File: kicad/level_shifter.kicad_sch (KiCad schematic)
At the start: 30 parts, among them U3 74LVC2T45GT, U4 74LVC2T45GT, U5 74LVC2T45GT, U6 74LVC2T45GT

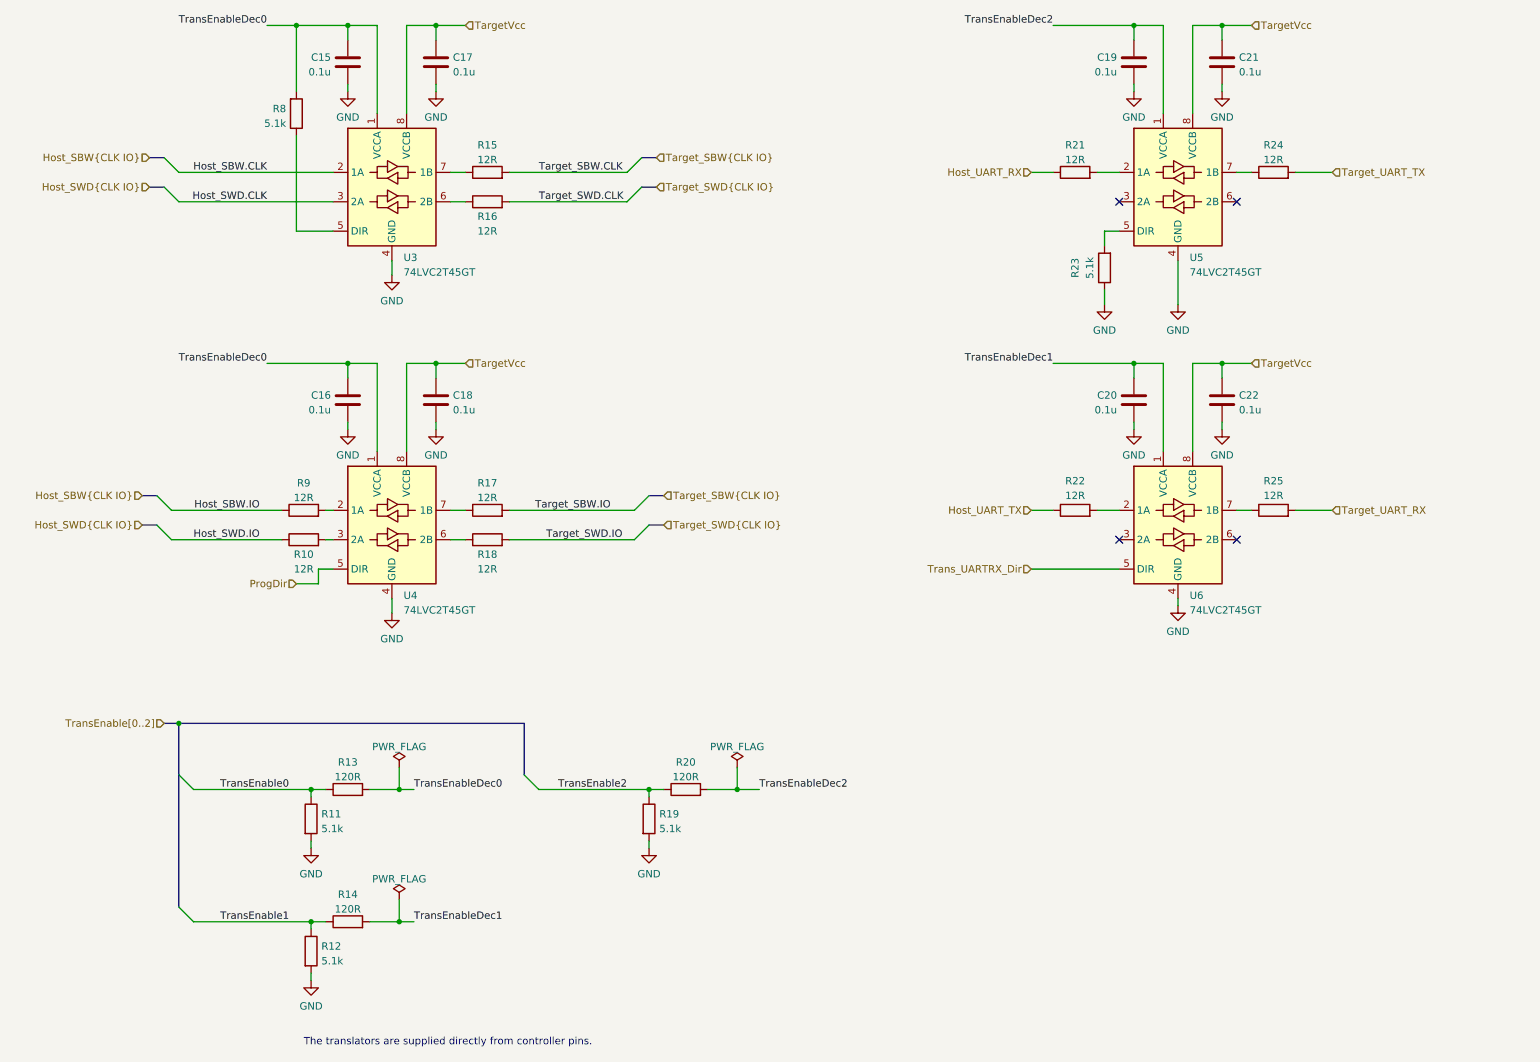
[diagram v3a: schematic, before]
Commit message: replace target supply diode with analog switch
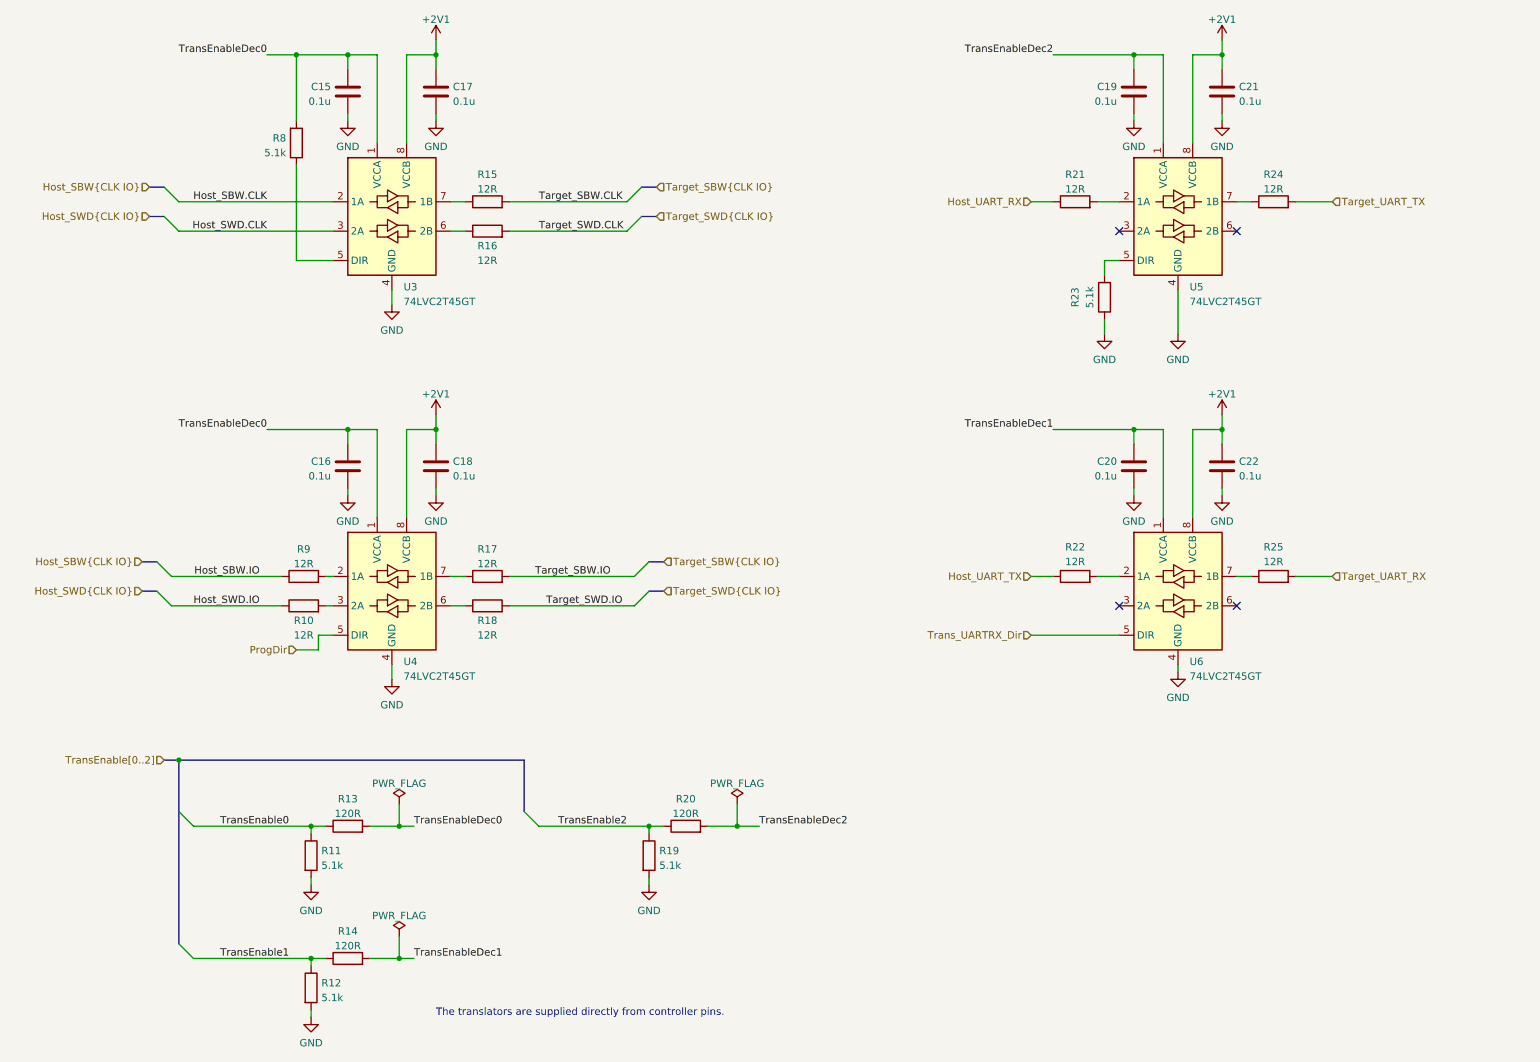
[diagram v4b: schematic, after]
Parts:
- C15, C16, C17, C18, C19, C20, C21, C22: MPN (none) -> CL05A104KA5NNNC
- R10, R15, R16, R17, R18, R21, R22, R24, R25, R9: MPN (none) -> RMCF0402FT12R0
- R11, R12, R19, R23, R8: MPN (none) -> CR0402-FX-5101GLF
- R13, R14, R20: MPN (none) -> CR0402-FX-1200GLF
- U3, U4, U5, U6: MPN (none) -> 74LVC2T45GT,115
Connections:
- net TargetVcc renamed +2V1
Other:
- moved on the sheet: C15, C16, C17, C18, C19, C20, C21, C22, R10, R11, R12, R13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
